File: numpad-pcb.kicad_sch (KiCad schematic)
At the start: 0 parts

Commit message: Complete MCU schematic
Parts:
- added C1: 1uF, symbol Device:C_Small
- added C2, C3, C4: 0.1uF, symbol Device:C_Small
- added C5: 10uF, symbol Device:C_Small
- added C6, C7: 22pF, symbol Device:C_Small
- added R1, R4: 10k, symbol Device:R_Small
- added R2, R3: 22, symbol Device:R_Small
- added SW1: SW_Push, symbol Switch:SW_Push
- added U1: ATmega32U4-A, Package_QFP:TQFP-44_10x10mm_P0.8mm, symbol MCU_Microchip_ATmega:ATmega32U4-A
- added Y1: Crystal_GND24_Small, symbol Device:Crystal_GND24_Small
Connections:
- new net: R1.1, U1.33 (~{HWB}/PE2)
- new net: R4.2, SW1.2, U1.13 (~{RESET})
- new net: C6.2, U1.17 (XTAL1), Y1.1
- new net: C7.2, U1.16 (XTAL2), Y1.3
- new net: R3.2, U1.3 (D-)
- new net: R2.1, U1.4 (D+)
- new net: C1.1, U1.6 (UCAP)
- new net +5V: C2.1, C3.1, C4.1, C5.1, R4.1, U1.14 (VCC), U1.2 (UVCC), U1.24 (AVCC), U1.34 (VCC), U1.44 (AVCC), U1.7 (VBUS)
- new net D+: R2.2
- new net D-: R3.1
- new net GND: C1.2, C2.2, C3.2, C4.2, C5.2, C6.1, C7.1, R1.2, SW1.1, U1.15 (GND), U1.23 (GND), U1.35 (GND), U1.43 (GND), U1.5 (UGND), Y1.2, Y1.4

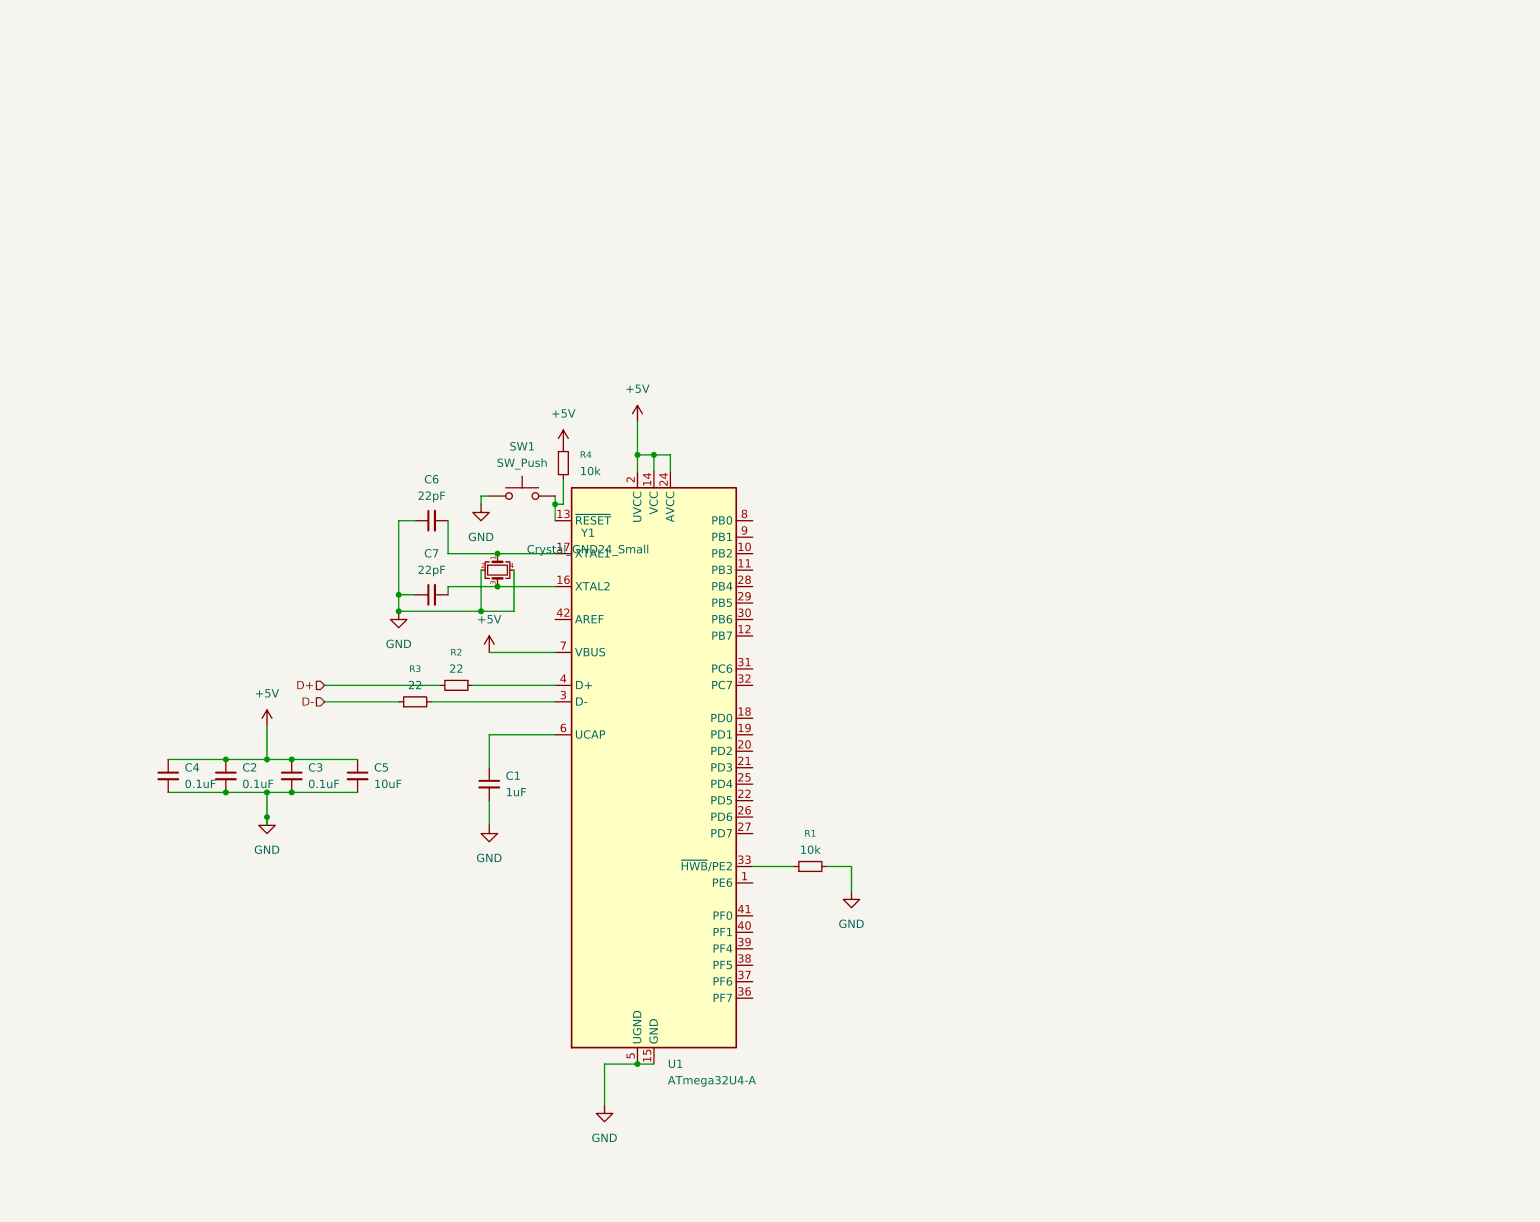
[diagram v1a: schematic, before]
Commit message: Add USB-C and reset schematic
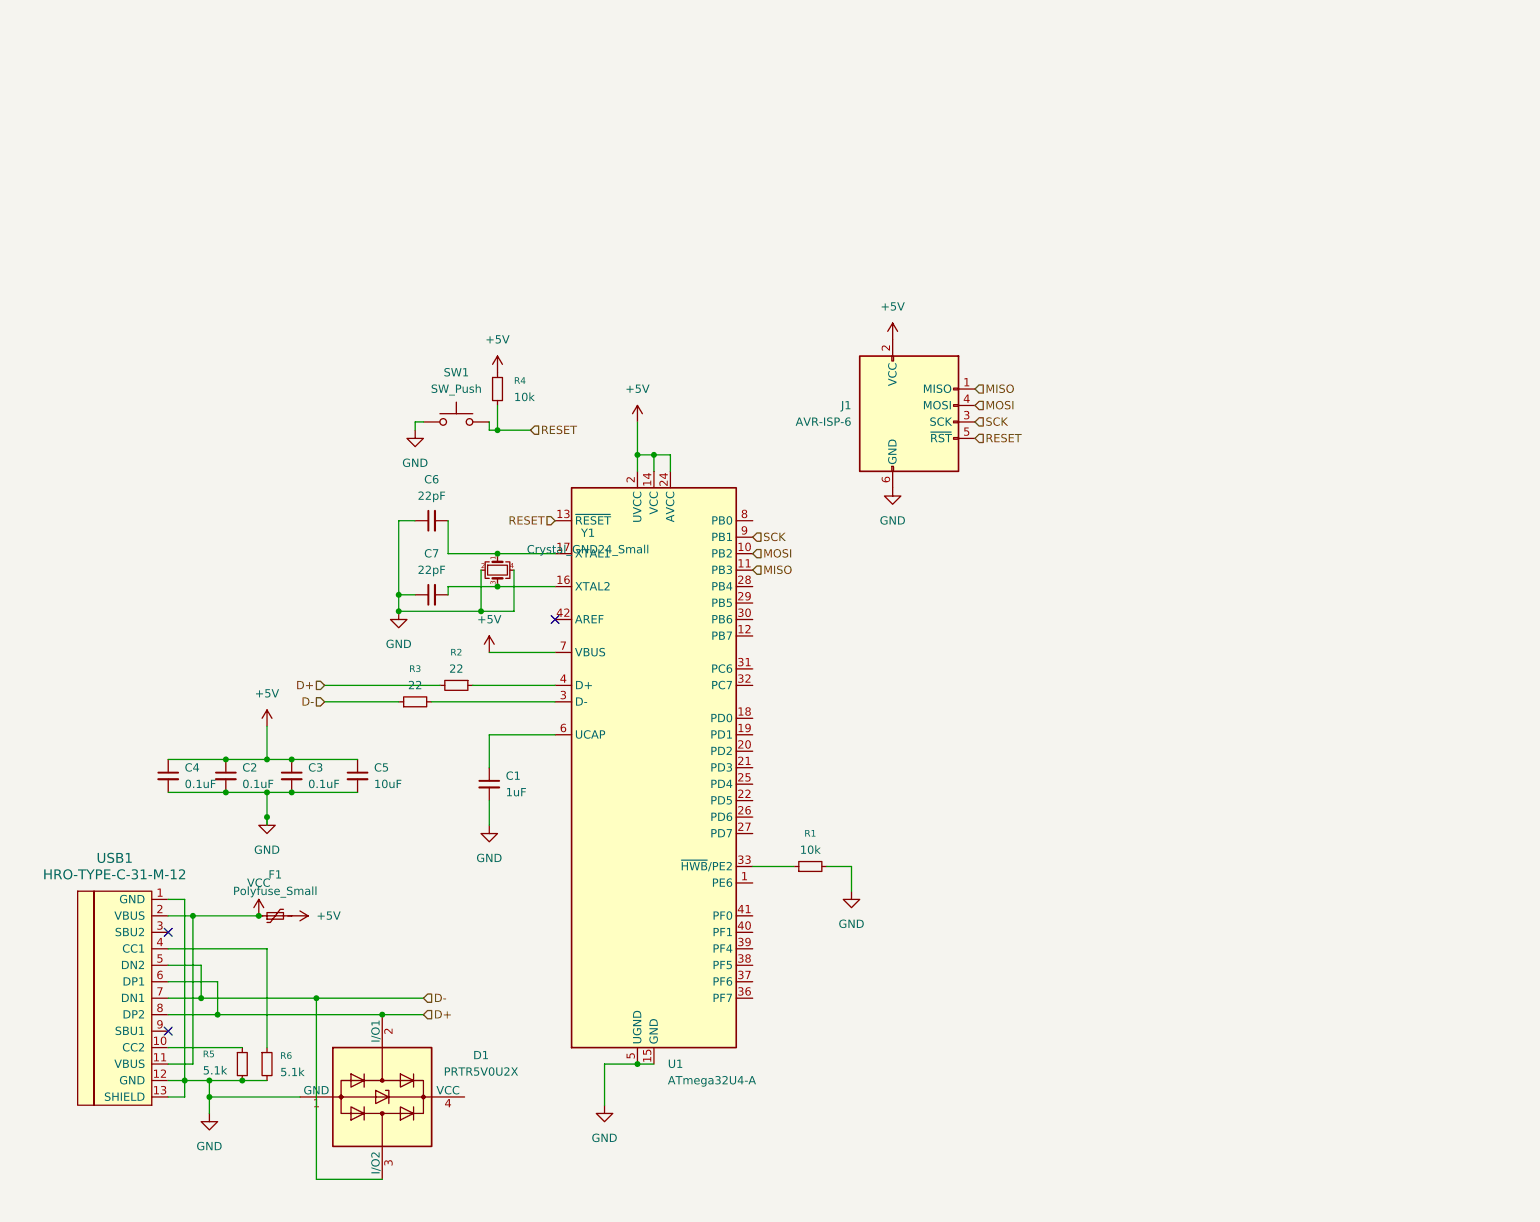
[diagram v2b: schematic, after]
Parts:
- added D1: PRTR5V0U2X, Package_TO_SOT_SMD:SOT-143, symbol Power_Protection:PRTR5V0U2X
- added F1: Polyfuse_Small, symbol Device:Polyfuse_Small
- added J1: AVR-ISP-6, symbol Connector:AVR-ISP-6
- added R5, R6: 5.1k, symbol Device:R_Small
- added USB1: HRO-TYPE-C-31-M-12, symbol Type-C:HRO-TYPE-C-31-M-12
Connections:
- net +5V: now also F1.2, J1.2 (VCC)
- net D+: now also D1.2 (I/O1), USB1.6 (DP1), USB1.8 (DP2)
- net D-: now also D1.3 (I/O2), USB1.5 (DN2), USB1.7 (DN1)
- net GND: now also D1.1 (GND), J1.6 (GND), R5.2, R6.2, USB1.1 (GND), USB1.12 (GND), USB1.13 (SHIELD)
- net RESET: now reaches R4.2, SW1.2, U1.13 (~{RESET})
- net RESET: now also J1.5 (~{RST})
- net MOSI: now reaches U1.10 (PB2)
- net MOSI: now also J1.4 (MOSI)
- net MISO: now reaches U1.11 (PB3)
- net MISO: now also J1.1 (MISO)
- net SCK: now reaches U1.9 (PB1)
- net SCK: now also J1.3 (SCK)
- new net: R5.1, USB1.10 (CC2)
- new net: R6.1, USB1.4 (CC1)
- new net VCC: F1.1, USB1.11 (VBUS), USB1.2 (VBUS)
- no-connect marks 0 -> 3
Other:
- moved on the sheet: R4, SW1

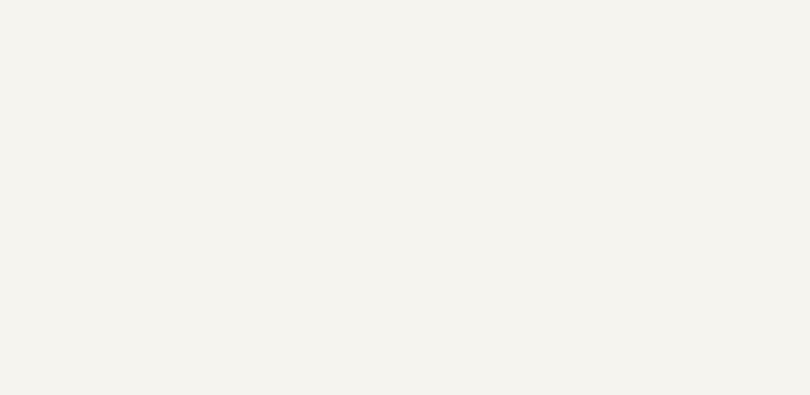
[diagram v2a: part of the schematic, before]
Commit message: Create numpad matrix
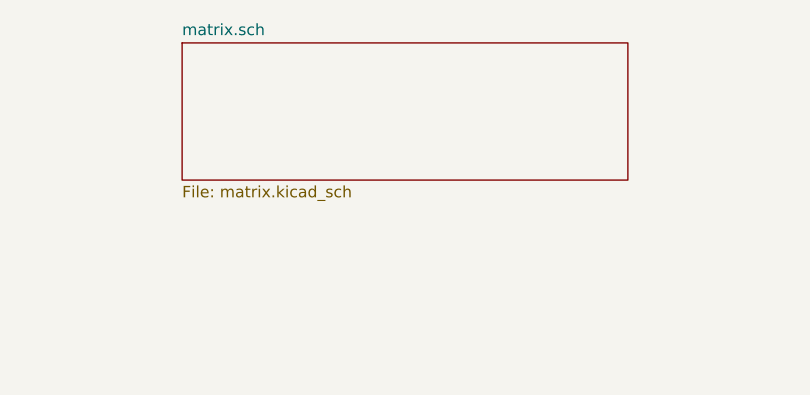
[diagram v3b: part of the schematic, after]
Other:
- added sheet matrix.sch (matrix.kicad_sch)
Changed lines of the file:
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@@
+		)
+	)
+	(sheet
+		(at 76.2 -26.035)
+		(size 49.53 15.24)
+		(exclude_from_sim no)
+		(in_bom yes)
+		(on_board yes)
+		(dnp no)
+		(fields_autoplaced yes)
+		(stroke
+			(width 0.1524)
+			(type solid)
+		)
+		(fill
+			(color 0 0 0 0.0000)
+		)
+		(property "Sheetname" "matrix.sch"
+			(at 76.2 -26.7466 0)
+			(effects
+				(font
+					(size 1.27 1.27)
+				)
+				(justify left bottom)
+			)
+		)
+		(property "Sheetfile" "matrix.kicad_sch"
+			(at 76.2 -10.2104 0)
+			(effects
+				(font
+					(size 1.27 1.27)
+				)
+				(justify left top)
+			)
+		)
+		(instances
+			(project "numpad-pcb"
+				(path "/2a659eb2-66e9-44ab-8b6b-d3474cdae4b3"
+					(page "2")
+				)
+			)
 		)
 	)

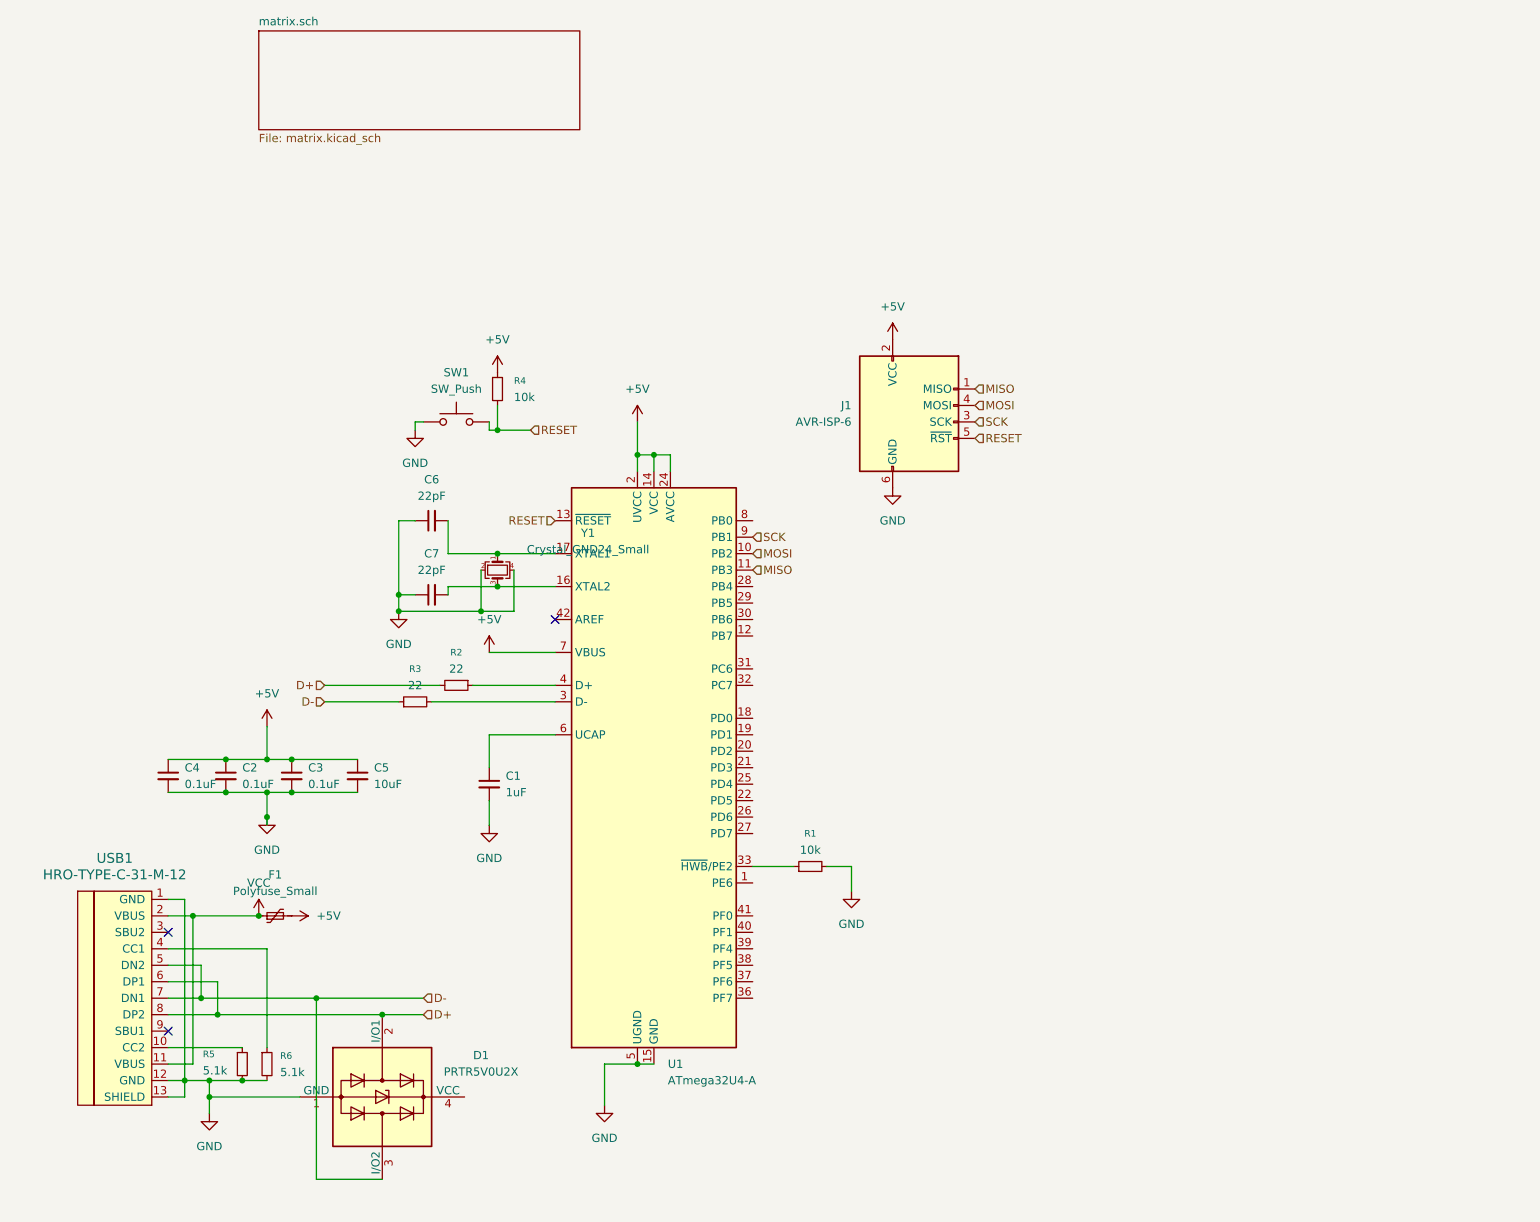
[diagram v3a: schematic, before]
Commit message: Fix schematic based on ERC
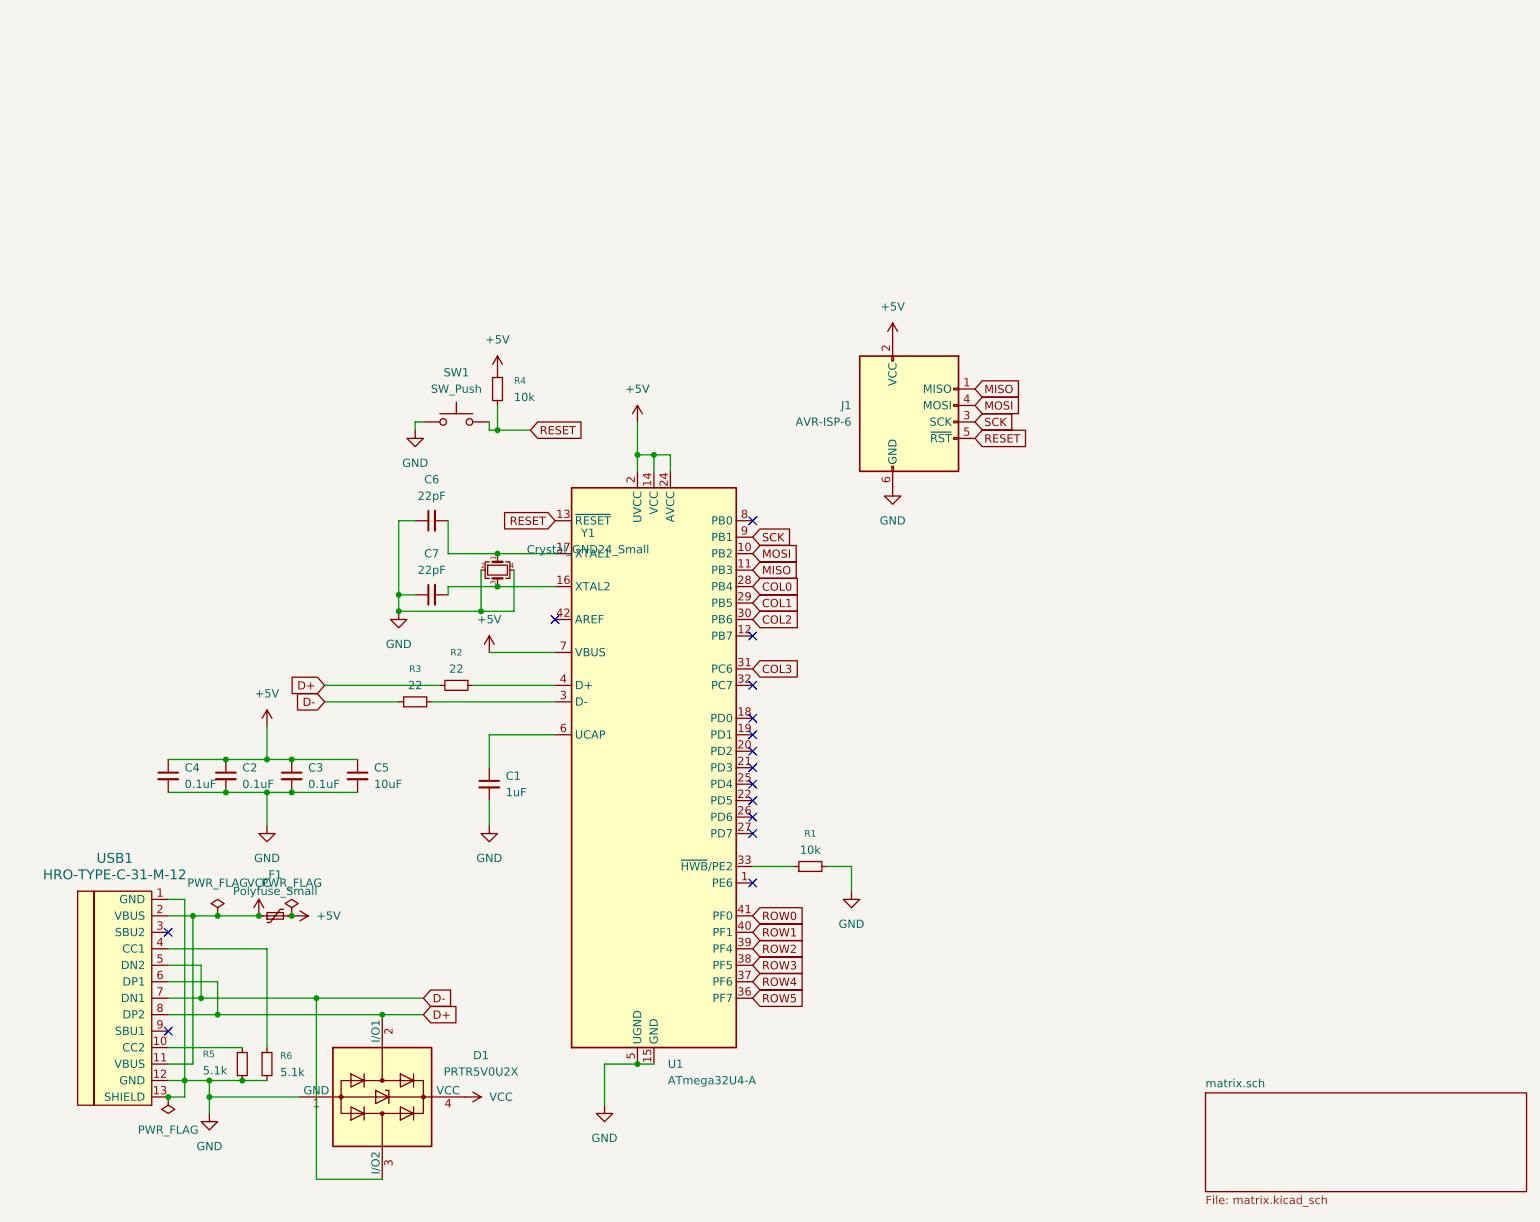
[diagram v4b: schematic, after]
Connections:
- net VCC: now also D1.4 (VCC)
- net COL0: now reaches U1.28 (PB4)
- net COL1: now reaches U1.29 (PB5)
- net COL2: now reaches U1.30 (PB6)
- net COL3: now reaches U1.31 (PC6)
- net ROW5: now reaches U1.36 (PF7)
- net ROW4: now reaches U1.37 (PF6)
- net ROW3: now reaches U1.38 (PF5)
- net ROW2: now reaches U1.39 (PF4)
- net ROW1: now reaches U1.40 (PF1)
- net ROW0: now reaches U1.41 (PF0)
- no-connect marks 3 -> 15
